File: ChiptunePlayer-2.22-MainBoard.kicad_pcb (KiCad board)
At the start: 2 copper layers, 7 parts, among them J1 USB_OTG

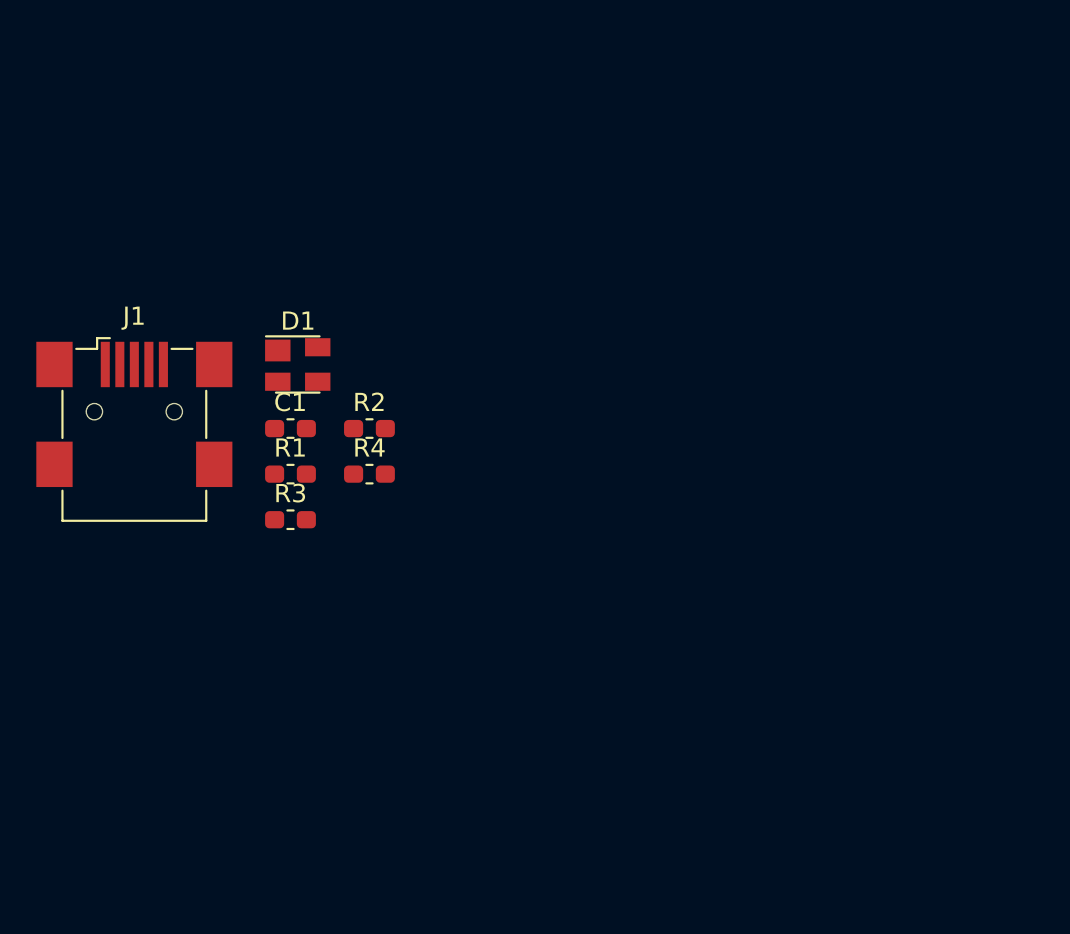
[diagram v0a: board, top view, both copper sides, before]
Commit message: Добавлена часть зарядки, клавиши +-, поправлен USB, все разделено на вложенные листи.
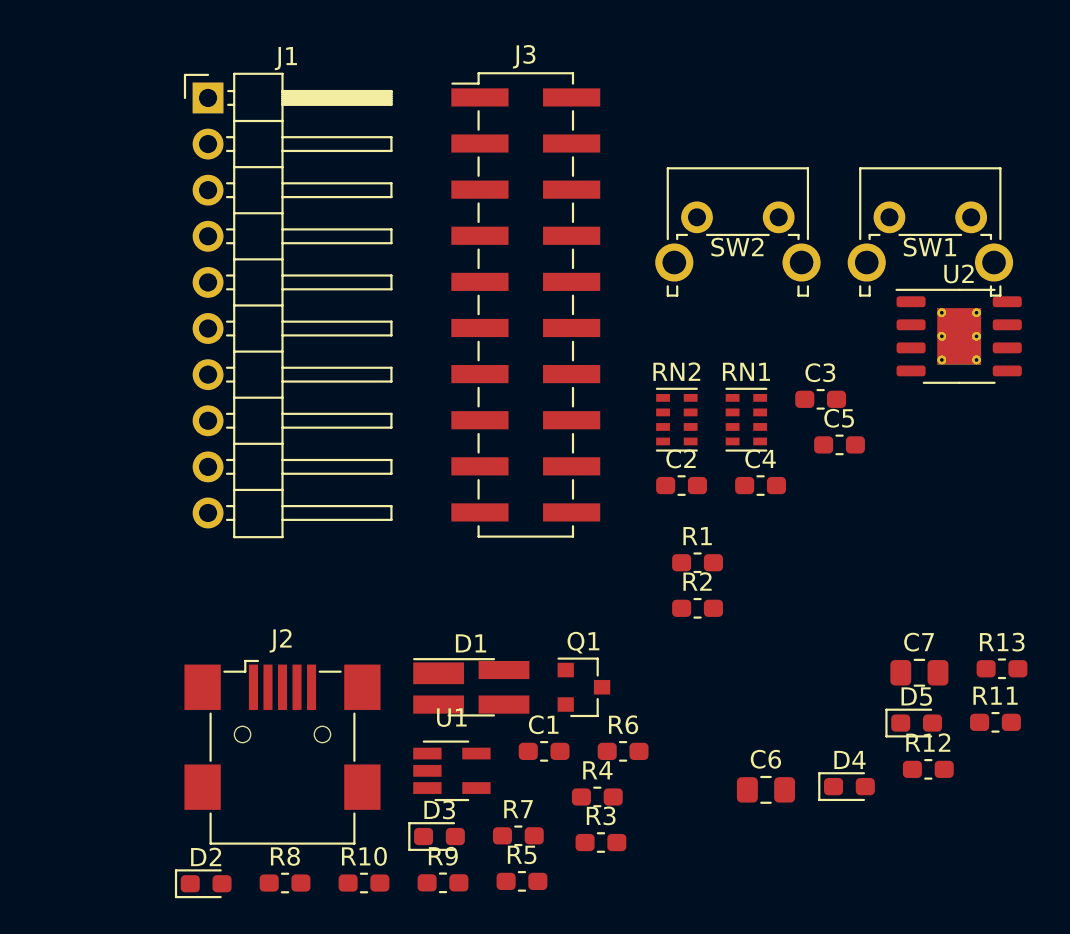
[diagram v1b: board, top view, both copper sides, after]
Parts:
- added C2: 100nF, Capacitor_SMD:C_0603_1608Metric_Pad1.05x0.95mm_HandSolder, F.Cu at (111.7, 70.5)
- added C3: 100nF, Capacitor_SMD:C_0603_1608Metric_Pad1.05x0.95mm_HandSolder, F.Cu at (119.4, 65.7)
- added C4: 100nF, Capacitor_SMD:C_0603_1608Metric_Pad1.05x0.95mm_HandSolder, F.Cu at (116.1, 70.5)
- added C5: 100nF, Capacitor_SMD:C_0603_1608Metric_Pad1.05x0.95mm_HandSolder, F.Cu at (120.4, 68.2)
- added C6: 10uF, Capacitor_SMD:C_0805_2012Metric_Pad1.15x1.40mm_HandSolder, F.Cu at (116.4, 87.2)
- added C7: 10uF, Capacitor_SMD:C_0805_2012Metric_Pad1.15x1.40mm_HandSolder, F.Cu at (124.8, 80.8)
- added D2: RED, LED_SMD:LED_0603_1608Metric_Pad1.05x0.95mm_HandSolder, F.Cu at (85.5, 92.4)
- added D3: GREEN, LED_SMD:LED_0603_1608Metric_Pad1.05x0.95mm_HandSolder, F.Cu at (98.4, 89.8)
- added D4: CHRG, LED_SMD:LED_0603_1608Metric_Pad1.05x0.95mm_HandSolder, F.Cu at (121.0, 87.0)
- added D5: STDBY, LED_SMD:LED_0603_1608Metric_Pad1.05x0.95mm_HandSolder, F.Cu at (124.7, 83.5)
- added J2: USB_OTG, Connector_USB:USB_Mini-B_Wuerth_65100516121_Horizontal, F.Cu at (89.7, 84.2)
- added J3: Conn_02x10_Odd_Even, Connector_PinHeader_2.54mm:PinHeader_2x10_P2.54mm_Vertical_SMD, F.Cu at (103.1, 60.5)
- added Q1: BC817, Package_TO_SOT_SMD:SOT-23, F.Cu at (106.3, 81.6)
- added R10: 10K, Resistor_SMD:R_0603_1608Metric_Pad1.05x0.95mm_HandSolder, F.Cu at (94.2, 92.3)
- added R11: 1K2, Resistor_SMD:R_0603_1608Metric_Pad1.05x0.95mm_HandSolder, F.Cu at (129.0, 83.5)
- added R12: 330, Resistor_SMD:R_0603_1608Metric_Pad1.05x0.95mm_HandSolder, F.Cu at (125.3, 86.1)
- added R13: 330, Resistor_SMD:R_0603_1608Metric_Pad1.05x0.95mm_HandSolder, F.Cu at (129.4, 80.5)
- added R5: 330, Resistor_SMD:R_0603_1608Metric_Pad1.05x0.95mm_HandSolder, F.Cu at (102.9, 92.2)
- added R6: 330, Resistor_SMD:R_0603_1608Metric_Pad1.05x0.95mm_HandSolder, F.Cu at (108.5, 85.1)
- added R7: 22, Resistor_SMD:R_0603_1608Metric_Pad1.05x0.95mm_HandSolder, F.Cu at (102.7, 89.7)
- added R8: 22, Resistor_SMD:R_0603_1608Metric_Pad1.05x0.95mm_HandSolder, F.Cu at (89.9, 92.3)
- added R9: 10K, Resistor_SMD:R_0603_1608Metric_Pad1.05x0.95mm_HandSolder, F.Cu at (98.6, 92.3)
- added RN1: CAT16-103J4, Resistor_SMD:R_Cat16-4, F.Cu at (115.3, 66.8)
- added RN2: CAT16-103J4, Resistor_SMD:R_Cat16-4, F.Cu at (111.5, 66.8)
- added SW1: UP, Button_Switch_THT:SW_Tactile_SPST_Angled_PTS645Vx83-2LFS, F.Cu at (123.2, 55.7)
- added SW2: DOWN, Button_Switch_THT:SW_Tactile_SPST_Angled_PTS645Vx83-2LFS, F.Cu at (112.6, 55.7)
- added U1: STMPS2151STR, Package_TO_SOT_SMD:SOT-23-5_HandSoldering, F.Cu at (99.1, 86.2)
- added U2: TP4056, Package_SO:HSOP-8-1EP_3.9x4.9mm_P1.27mm_EP2.41x3.1mm_ThermalVias, F.Cu at (127.0, 62.2)
- C1: value 100nF -> 4.7uF
- D1: footprint Package_TO_SOT_SMD:SOT-143 -> Package_TO_SOT_SMD:SOT-143_Handsoldering
- J1: value USB_OTG -> Conn_01x10_Male; footprint Connector_USB:USB_Mini-B_Wuerth_65100516121_Horizontal -> Connector_PinHeader_2.54mm:PinHeader_1x10_P2.54mm_Horizontal
- R3: value 22 -> 1K
- R4: value 22 -> 10K
- moved R3 24.7 mm to (107.3, 90.1)
- moved R1 22.9 mm to (112.6, 74.7)
- moved C1 22.6 mm to (104.1, 85.1)
- moved R4 21.8 mm to (107.1, 87.6)
- moved R2 20.6 mm to (112.6, 77.2)
- moved D1 20.2 mm to (100.1, 81.6)
- moved J1 17.8 mm to (85.6, 49.1)
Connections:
- C1 pad 1: ADC_BAT -> /USB_OTG_VBUS
- D1 pad 4: USB_ID -> /usb/ID
- J1 pad 1: (no net) -> GND
- J1 pad 2: Net-(D1-Pad3) -> +3V3
- J1 pad 3: Net-(D1-Pad2) -> (no net)
- J1 pad 4: USB_ID -> (no net)
- J1 pad 5: GND -> (no net)
- J1 pad 6: GND -> (no net)
- R1 pad 1: (no net) -> /buttons/BUTTON_UP
- R1 pad 2: ADC_BAT -> +3V3
- R2 pad 1: ADC_BAT -> /buttons/BUTTON_DOWN
- R2 pad 2: GND -> +3V3
- R3 pad 1: Net-(D1-Pad2) -> Net-(Q1-Pad1)
- R3 pad 2: (no net) -> /USB_OTG_VBUS
- R4 pad 1: Net-(D1-Pad3) -> GND
- R4 pad 2: (no net) -> Net-(Q1-Pad1)

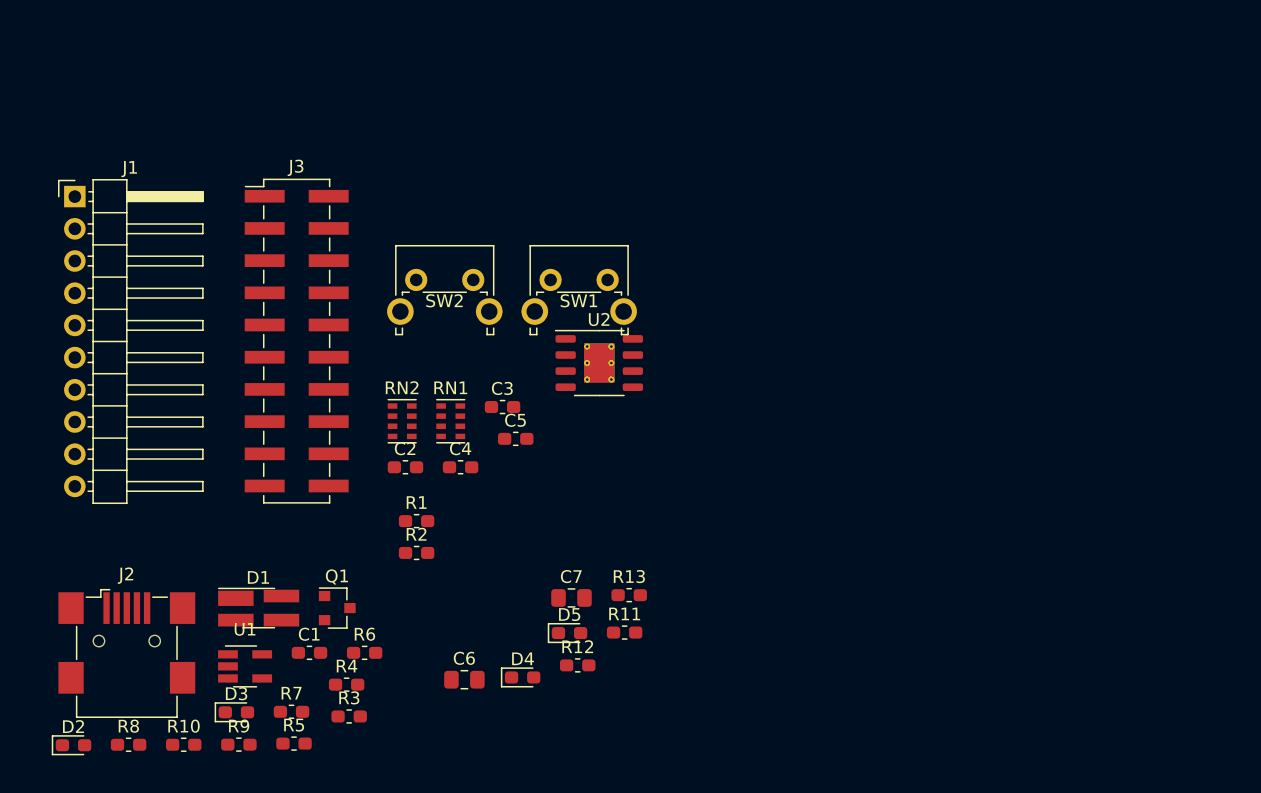
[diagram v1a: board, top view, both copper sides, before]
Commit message: Запитал МК, добавил цепи питания, тактирования, модуль клавиатуры.
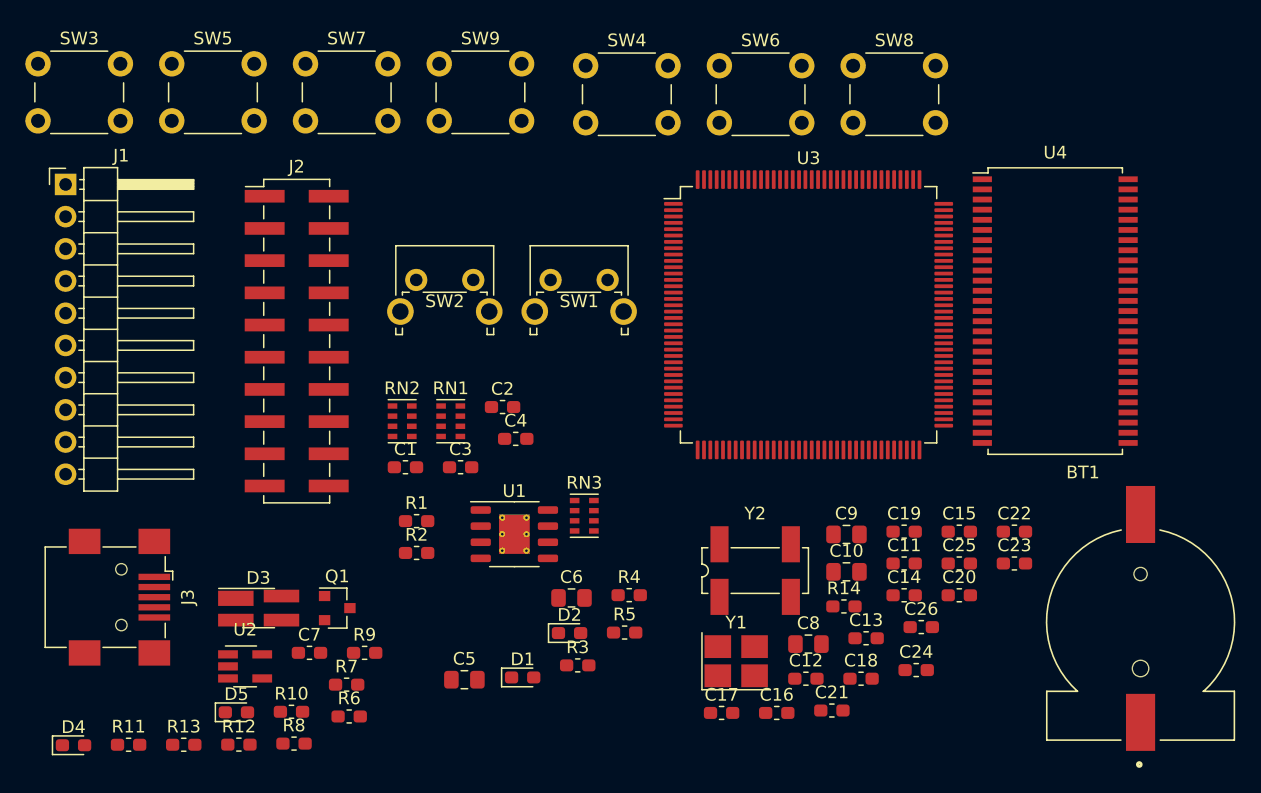
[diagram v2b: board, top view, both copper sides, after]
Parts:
- added BT1: S8411-45R, bat:BAT_S8411-45R, F.Cu at (169.7, 82.6)
- added C10: 1uF, Capacitor_SMD:C_0805_2012Metric_Pad1.15x1.40mm_HandSolder, F.Cu at (146.5, 78.7)
- added C11: 100nF, Capacitor_SMD:C_0603_1608Metric_Pad1.05x0.95mm_HandSolder, F.Cu at (151.1, 78.0)
- added C12: 100nF, Capacitor_SMD:C_0603_1608Metric_Pad1.05x0.95mm_HandSolder, F.Cu at (143.3, 87.1)
- added C13: 100nF, Capacitor_SMD:C_0603_1608Metric_Pad1.05x0.95mm_HandSolder, F.Cu at (148.1, 83.9)
- added C14: 100nF, Capacitor_SMD:C_0603_1608Metric_Pad1.05x0.95mm_HandSolder, F.Cu at (151.1, 80.5)
- added C15: 100nF, Capacitor_SMD:C_0603_1608Metric_Pad1.05x0.95mm_HandSolder, F.Cu at (155.4, 75.5)
- added C16: 100nF, Capacitor_SMD:C_0603_1608Metric_Pad1.05x0.95mm_HandSolder, F.Cu at (141.0, 89.8)
- added C17: 100nF, Capacitor_SMD:C_0603_1608Metric_Pad1.05x0.95mm_HandSolder, F.Cu at (136.7, 89.8)
- added C18: 100nF, Capacitor_SMD:C_0603_1608Metric_Pad1.05x0.95mm_HandSolder, F.Cu at (147.7, 87.1)
- added C19: 100nF, Capacitor_SMD:C_0603_1608Metric_Pad1.05x0.95mm_HandSolder, F.Cu at (151.1, 75.5)
- added C20: 100nF, Capacitor_SMD:C_0603_1608Metric_Pad1.05x0.95mm_HandSolder, F.Cu at (155.4, 80.5)
- added C21: 100nF, Capacitor_SMD:C_0603_1608Metric_Pad1.05x0.95mm_HandSolder, F.Cu at (145.3, 89.6)
- added C22: 22, Capacitor_SMD:C_0603_1608Metric_Pad1.05x0.95mm_HandSolder, F.Cu at (159.8, 75.5)
- added C23: 22, Capacitor_SMD:C_0603_1608Metric_Pad1.05x0.95mm_HandSolder, F.Cu at (159.8, 78.0)
- added C24: 22, Capacitor_SMD:C_0603_1608Metric_Pad1.05x0.95mm_HandSolder, F.Cu at (152.0, 86.5)
- added C25: 22, Capacitor_SMD:C_0603_1608Metric_Pad1.05x0.95mm_HandSolder, F.Cu at (155.4, 78.0)
- added C26: 100nF, Capacitor_SMD:C_0603_1608Metric_Pad1.05x0.95mm_HandSolder, F.Cu at (152.4, 83.1)
- added C8: 2.2uF, Capacitor_SMD:C_0805_2012Metric_Pad1.15x1.40mm_HandSolder, F.Cu at (143.5, 84.4)
- added C9: 2.2uF, Capacitor_SMD:C_0805_2012Metric_Pad1.15x1.40mm_HandSolder, F.Cu at (146.5, 75.8)
- added R14: 10K, Resistor_SMD:R_0603_1608Metric_Pad1.05x0.95mm_HandSolder, F.Cu at (146.3, 81.4)
- added RN3: CAT16-103J4, Resistor_SMD:R_Cat16-4, F.Cu at (125.8, 74.3)
- added SW3: MENY, Button_Switch_THT:SW_PUSH_6mm_H13mm, F.Cu at (82.7, 38.6)
- added SW4: LEFT, Button_Switch_THT:SW_PUSH_6mm_H13mm, F.Cu at (125.9, 38.8)
- added SW5: UP, Button_Switch_THT:SW_PUSH_6mm_H13mm, F.Cu at (93.3, 38.6)
- added SW6: ENTER, Button_Switch_THT:SW_PUSH_6mm_H13mm, F.Cu at (136.5, 38.8)
- added SW7: DOWN, Button_Switch_THT:SW_PUSH_6mm_H13mm, F.Cu at (103.8, 38.6)
- added SW8: RETURN, Button_Switch_THT:SW_PUSH_6mm_H13mm, F.Cu at (147.0, 38.8)
- added SW9: RIGHT, Button_Switch_THT:SW_PUSH_6mm_H13mm, F.Cu at (114.4, 38.6)
- added U3: STM32F722ZETx, Package_QFP:LQFP-144_20x20mm_P0.5mm, F.Cu at (143.5, 58.4)
- added U4: W9812G6KH-6, Package_SO:TSOP-II-54_22.2x10.16mm_P0.8mm, F.Cu at (163.0, 58.1)
- added Y1: NX3225SA-16.000M-STD-CRS-2, Crystal:Crystal_SMD_3225-4Pin_3.2x2.5mm_HandSoldering, F.Cu at (137.8, 85.8)
- added Y2: MC-306, Crystal:Crystal_SMD_SeikoEpson_MC306-4Pin_8.0x3.2mm_HandSoldering, F.Cu at (139.3, 78.6)
- SW1: value UP -> +
- SW2: value DOWN -> -
- moved U1 15.1 mm to (120.3, 75.7)
- moved J3 3.49 mm to (89.3, 80.7), turned to 270 degrees
- moved J1 1.21 mm to (84.9, 48.1)
- renumbered C2 to C1, C3 to C2, C4 to C3, C5 to C4, C6 to C5, C7 to C6, C1 to C7, D4 to D1, D5 to D2, D1 to D3, D2 to D4, D3 to D5, J3 to J2, J2 to J3, R7 to R10, R8 to R11, R9 to R12, R10 to R13, R12 to R3, R13 to R4, R11 to R5, R3 to R6, R4 to R7, R5 to R8, R6 to R9, U2 to U1, U1 to U2
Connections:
- net /usb/ID renamed /USB_ID
- net /usb/OTG_EN renamed /OTG_EN
- net /usb/VBUT_FAULT renamed /VBUS_FAULT
- net Net-(D1-Pad2) renamed /usb/U_DP_+
- net Net-(D1-Pad3) renamed /usb/U_DP_-
- J1 pad 1: GND -> GNDD
- J1 pad 10: (no net) -> /mc/JT_MS
- J1 pad 2: +3V3 -> VDD
- J1 pad 3: (no net) -> /mc/NRST
- J1 pad 6: (no net) -> /mc/JT_RST
- J1 pad 7: (no net) -> /mc/JT_DO
- J1 pad 8: (no net) -> /mc/JT_DI
- J1 pad 9: (no net) -> /mc/JT_CLK
- R10 pad 2: (no net) -> /USB_D_+
- R11 pad 2: (no net) -> /USB_D_-
